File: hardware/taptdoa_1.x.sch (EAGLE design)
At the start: 67 parts, among them J1 105017-0001, U1 AP2112K-3.3TRG1, U2 STM32F103RBT6, Y1 8MHz

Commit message: v1.2 of board
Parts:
- removed TP21, TP22, TP4, TP5, TP6, TP7: TEST-POINT3X4, SparkFun-Connectors:TEST-POINT3X4
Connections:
- removed net PC0: R1.1, U2.PC0
- removed net PC1: R2.1, U2.PC1
- removed net PC2: R5.1, U2.PC2
- removed net PC3: R3.1, U2.PC3
- removed net PC4: R4.1, U2.PC4
- removed net PC5: R6.1, U2.PC5
- net OPAMP3_OUT: now also TP2.1; no longer TP21.1
- net PB2: now also TP3.1; no longer TP22.1
- net PB3: now also R1.1; no longer TP7.1
- net PB4: now also R2.1; no longer TP6.1
- net PB5: now also R5.1; no longer TP5.1
- net PB6: now also R3.1; no longer TP4.1
- net PB7: now also R4.1; no longer TP3.1
- net PB8: now also R6.1; no longer TP2.1
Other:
- moved on the sheet: C5, C9, J2, R1, R2, R3, R4, R5, R6, TP2, TP3

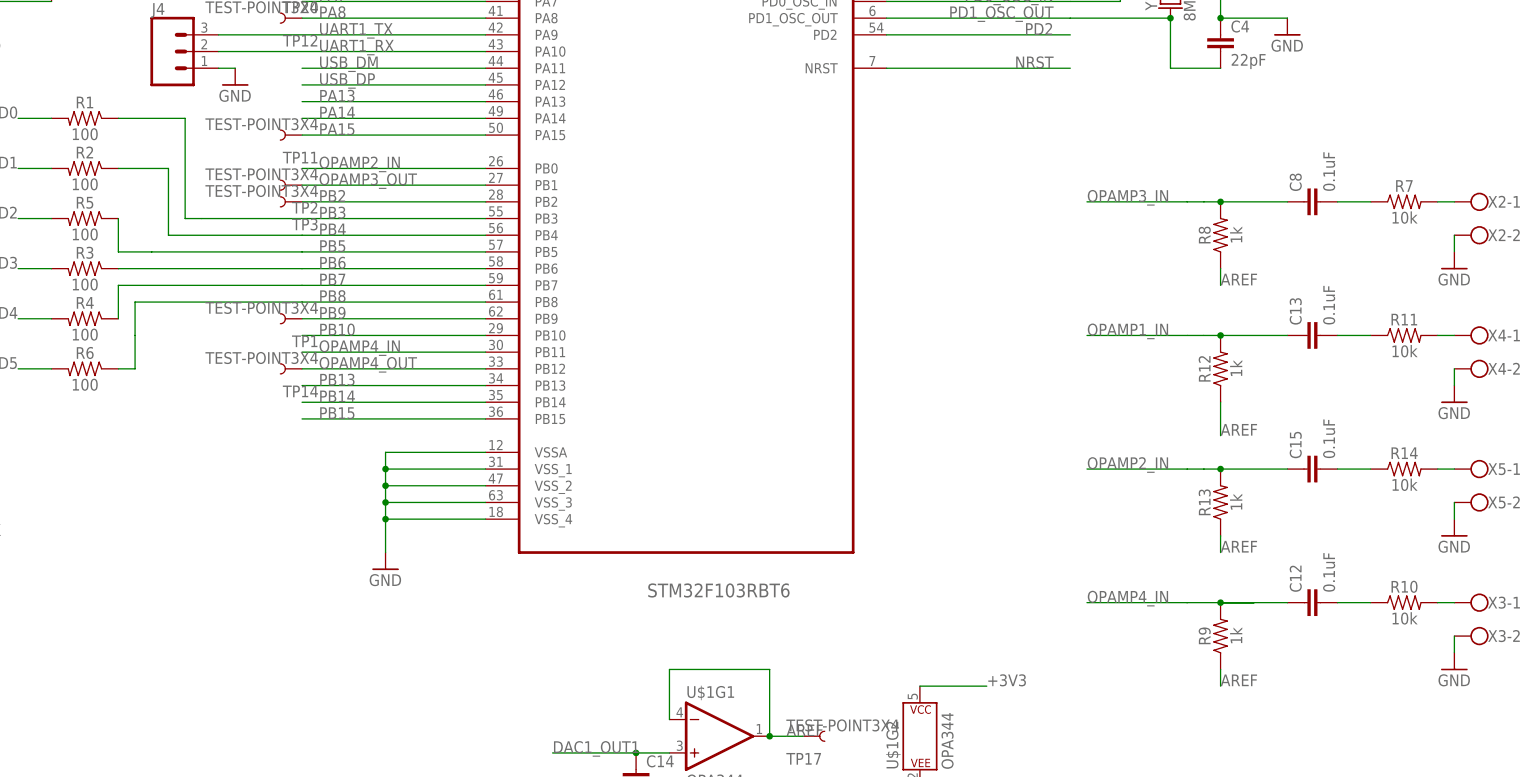
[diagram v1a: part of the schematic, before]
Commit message: working on LEDs, simple threshold detection for now, limited filtering
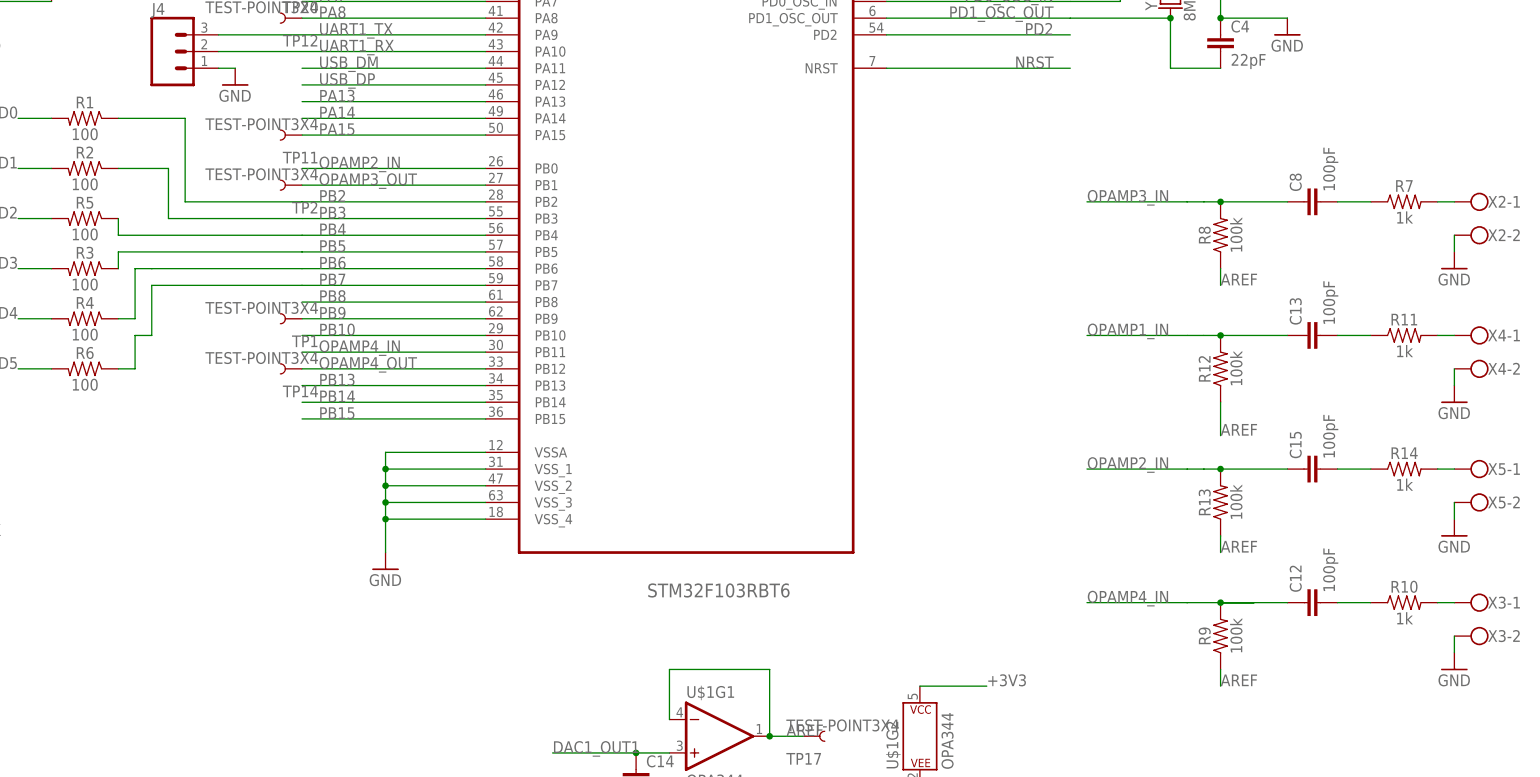
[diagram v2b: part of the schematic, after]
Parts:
- removed TP3: TEST-POINT3X4, SparkFun-Connectors:TEST-POINT3X4
- C12, C13, C15, C8: value 0.1uF -> 100pF
- R10, R11, R14, R7: value 10k -> 1k
- R12, R13, R8, R9: value 1k -> 100k
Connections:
- net PB2: now also R1.1; no longer TP3.1
- net PB3: now also R2.1; no longer R1.1
- net PB4: now also R5.1; no longer R2.1
- net PB5: now also R3.1; no longer R5.1
- net PB6: now also R4.1; no longer R3.1
- net PB7: now also R6.1; no longer R4.1
- net PB8: no longer R6.1

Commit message: re layout board
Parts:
- removed C14: 0.1uF, SparkFun-Capacitors:0.1UF-0603-25V-5%
- removed TP13, TP14, TP15, TP16, TP18, TP19, TP20: TEST-POINT3X4, SparkFun-Connectors:TEST-POINT3X4
- removed X1, X2, X3, X4, X5: (no value), con-wago-500:W237-102
- added C16: 0.1uF, SparkFun-Capacitors:0.1UF-0603-25V-5%
- added C17: 1.0uF, SparkFun-Capacitors:1.0UF-0603-16V-10%
- added C18, C19, C20, C21, C22, C23, C24, C25: 1nF, SparkFun-Capacitors:1.0UF-0603-16V-10%
- added C26, C27: 100uF, SparkFun-Capacitors:100UF-POLAR-25V-20%(ELEC)
- added FB2, FB3, FB4, FB5, FB6: 30Ω/1.8A, SparkFun-Coils:FERRITE_BEAD-0603
- added J6, J7: (no value), SparkFun-Connectors:CONN_04LOCK_LONGPADS
- added L1: 3.3µH/±20%/450mA, SparkFun-Coils:INDUCTOR-0805-3.3UH
- added R16, R17: 33, SparkFun-Resistors:100OHM-0603-1/4W-5%
- added R18, R19: 75, SparkFun-Resistors:100OHM-0603-1/4W-5%
- added TP3, TP4, TP5, TP6, TP7: TEST-POINT3X4, SparkFun-Connectors:TEST-POINT3X4
- added U$2: XT30XT30_THRUHOLE, XT30Male:XT30XT30_THRUHOLE
- added U4: SN74HCT245PWR, scanlime:74245PW
- C12, C13, C15, C8: value 100pF -> 1nF
- C3: value 1.0uF -> 4.7uF
- J3: device SparkFun-Connectors:CONN_09LOCK-LONGPADS -> SparkFun-Connectors:CONN_18
- J5: device SparkFun-Connectors:CONN_09LOCK-LONGPADS -> SparkFun-Connectors:CONN_06LOCK
- R1, R2, R3, R4, R5, R6: value 100 -> 75
- R10, R11, R14, R7: value 1k -> 10k
- R12, R13, R8, R9: value 100k -> 10k
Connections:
- removed net +5V: J3.3, J3.6, J3.9, J5.3, J5.6, J5.9, X1-1.KL
- removed net DAC1_OUT2: TP19.1, U2.PA5
- removed net N$1: R7.2, X2-1.KL
- removed net N$3: R11.2, X4-1.KL
- removed net N$5: R14.2, X5-1.KL
- removed net N$7: C12.2, R10.1
- removed net OPAMP1_IN: C13.1, R12.2, U2.PA3
- removed net OPAMP1_OUT: TP18.1, U2.PA2
- removed net OPAMP2_IN: C15.1, R13.2, U2.PB0
- removed net OPAMP2_OUT: TP20.1, U2.PA6
- removed net OPAMP3_IN: C8.1, R8.2, U2.PA1
- removed net OPAMP3_OUT: TP2.1, U2.PB1
- removed net OPAMP4_IN: C12.1, R9.2, U2.PB11
- removed net OPAMP4_OUT: TP14.1, U2.PB12
- removed net PA0-WKUP: U2.PA0-WKUP
- removed net PA15: TP11.1, U2.PA15
- removed net PA7: U2.PA7
- removed net PA8: TP12.1, U2.PA8
- removed net PB10: U2.PB10
- removed net PB13: U2.PB13
- removed net PB14: U2.PB14
- removed net PB15: U2.PB15
- removed net PB2: R1.1, U2.PB2
- removed net PB3: R2.1, U2.PB3
- removed net PB4: R5.1, U2.PB4
- removed net PB5: R3.1, U2.PB5
- removed net PB6: R4.1, U2.PB6
- removed net PB7: R6.1, U2.PB7
- removed net PB8: U2.PB8
- removed net PB9: TP1.1, U2.PB9
- removed net PC10: TP10.1, U2.PC10
- removed net PC11: TP9.1, U2.PC11
- removed net PC12: TP8.1, U2.PC12
- removed net PC13-TAMPER-RTC: U2.PC13-TAMPER-RTC
- removed net PC14-OSC32_IN: U2.PC14-OSC32_IN
- removed net PC15-OSC32_OUT: U2.PC15-OSC32_OUT
- removed net PC6: TP16.1, U2.PC6
- removed net PC7: TP13.1, U2.PC7
- removed net PC8: TP15.1, U2.PC8
- removed net PC9: U2.PC9
- removed net PD2: U2.PD2
- removed net VBAT: U2.VBAT
- new net 5V: C26.+, C27.+, J3.1, J3.10, J3.13, J3.16, J3.4, J3.7, J5.1, J5.4, U$2.5V, U4.DIR, U4.VCC
- new net HP1: C8.1, R7.2, R8.2, TP9.1
- new net HP2: C13.1, R11.2, R12.2, TP10.1
- new net HP3: C15.1, R13.2, R14.2, TP11.1
- new net HP4: C12.1, R10.2, R9.2, TP12.1
- new net N$10: R17.1, U2.PA12
- new net N$11: FB2.1, J1.GND
- new net N$12: C17.1, L1.1, U1.OUT
- new net N$13: R1.1, U4.B1
- new net N$14: R2.1, U4.B2
- new net N$15: R5.1, U4.B3
- new net N$16: R3.1, U4.B4
- new net N$17: R4.1, U4.B5
- new net N$18: R6.1, U4.B6
- new net N$19: C8.2, FB3.1
- new net N$20: C15.2, FB5.1
- new net N$21: C13.2, FB4.1
- new net N$22: U2.PC12, U4.A4
- new net N$23: C12.2, FB6.1
- new net N$24: U2.PC13-TAMPER-RTC, U4.A3
- new net N$25: U2.PC14-OSC32_IN, U4.A2
- new net N$26: U2.PC15-OSC32_OUT, U4.A1
- new net N$27: R18.1, U4.B7
- new net N$28: R19.1, U4.B8
- new net N$29: J5.2, R18.2
- new net N$30: J5.5, R19.2
- new net N$31: FB3.2, J6.1
- new net N$32: FB5.2, J7.1
- new net N$33: FB6.2, J7.3
- new net N$34: FB4.2, J6.3
- new net N$9: R16.1, U2.PA11
- new net OA1NEG: C22.1, U2.PA3
- new net OA1OUT: C22.2, TP4.1, U2.PA2
- new net OA2NEG: C23.1, U2.PC5
- new net OA2OUT: C23.2, TP3.1, U2.PA6
- new net OA3NEG: C24.1, U2.PB2
- new net OA3OUT: C24.2, TP1.1, U2.PB1
- new net OA4NEG: C25.2, U2.PB10
- new net OA4OUT: C25.1, TP2.1, U2.PB12
- new net SENSE1: C18.2, R7.1, TP8.1, U2.PA0-WKUP, U2.PA1
- new net SENSE2: C19.2, R11.1, TP7.1, U2.PA7, U2.PC4
- new net SENSE3: C20.2, R14.1, TP6.1, U2.PB0, U2.PB13
- new net SENSE4: C21.2, R10.1, TP5.1, U2.PB11, U2.PB14
- net +3V3: now also L1.2; no longer U1.OUT
- net AREF: now also C18.1, C19.1, C20.1, C21.1
- net DAC1_OUT1: no longer C14.1
- net GND: now also C16.2, C17.2, C26.-, C27.-, FB2.2, J3.12, J3.15, J3.18, J3.3, J3.6, J3.9, J5.3, J5.6, J6.2, J6.4, J7.2, J7.4, U$2.GND, U4.GND, U4.OE; no longer C14.2, J1.GND, J3.1, J3.4, J3.7, J5.1, J5.4, J5.7, X1-2.KL, X2-2.KL, X3-2.KL, X4-2.KL, X5-2.KL
- net LED0: now also J3.2; no longer J3.8
- net LED2: now also J3.8; no longer J3.2
- net LED3: now also J3.11; no longer J5.8
- net LED4: now also J3.14; no longer J5.5
- net LED5: now also J3.17; no longer J5.2
- net N$2: now also U2.PC8, U4.A8; no longer C13.2, R11.1
- net N$4: now also U2.PC9, U4.A7; no longer C15.2, R14.1
- net N$6: now also U2.PC10, U4.A6; no longer R10.2, X3-1.KL
- net N$8: now also U2.PC11, U4.A5; no longer C8.2, R7.1
- net PA13: now also U2.PA15; no longer U2.PA13
- net USB_DM: now also R16.2; no longer U2.PA11
- net USB_DP: now also R17.2; no longer U2.PA12
- net VUSB2: now also C16.1
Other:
- note added: "Serial"
- moved on the sheet: C1, C12, C13, C15, C3, C4, C5, C7, C8, C9, J2, J4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

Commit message: cleanup renumber
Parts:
- removed C27: 100uF, SparkFun-Capacitors:100UF-POLAR-25V-20%(ELEC)
- removed TP17: TEST-POINT3X4, SparkFun-Connectors:TEST-POINT3X4
- removed U4: SN74HCT245PWR, scanlime:74245PW
- added C14: 1nF, SparkFun-Capacitors:1.0UF-0603-16V-10%
- added TP13: TEST-POINT3X4, SparkFun-Connectors:TEST-POINT3X4
- added U3: STM32F103RBT6, ST Microelctronics_By_element14_Batch_1:STM32F103RBT6
- C1: value 22pF -> 100uF; device SparkFun-Capacitors:22PF-0603-50V-5% -> SparkFun-Capacitors:100UF-POLAR-25V-20%(ELEC)
- C10: value 0.1uF -> 10nF; device SparkFun-Capacitors:0.1UF-0603-25V-5% -> SparkFun-Capacitors:10NF-0603-50V-10%
- C11: value 0.1uF -> 1.0uF; device SparkFun-Capacitors:0.1UF-0603-25V-5% -> SparkFun-Capacitors:1.0UF-0603-16V-10%
- C13, C19, C22: value 1nF -> 0.1uF; device SparkFun-Capacitors:1.0UF-0603-16V-10% -> SparkFun-Capacitors:0.1UF-0603-25V-5%
- C16: value 0.1uF -> 1nF; device SparkFun-Capacitors:0.1UF-0603-25V-5% -> SparkFun-Capacitors:1.0UF-0603-16V-10%
- C17: value 1.0uF -> 1nF
- C2: value 0.1uF -> 100uF; device SparkFun-Capacitors:0.1UF-0603-25V-5% -> SparkFun-Capacitors:100UF-POLAR-25V-20%(ELEC)
- C26: value 100uF -> 1nF; device SparkFun-Capacitors:100UF-POLAR-25V-20%(ELEC) -> SparkFun-Capacitors:1.0UF-0603-16V-10%
- C3: value 4.7uF -> 0.1uF; device SparkFun-Capacitors:1.0UF-0603-16V-10% -> SparkFun-Capacitors:0.1UF-0603-25V-5%
- C4: value 22pF -> 4.7uF; device SparkFun-Capacitors:22PF-0603-50V-5% -> SparkFun-Capacitors:4.7UF0603
- C5: value 10nF -> 1.0uF; device SparkFun-Capacitors:10NF-0603-50V-10% -> SparkFun-Capacitors:1.0UF-0603-16V-10%
- C6: value 0.1uF -> 4.7uF; device SparkFun-Capacitors:0.1UF-0603-25V-5% -> SparkFun-Capacitors:1.0UF-0603-16V-10%
- C7: value 4.7uF -> 0.1uF; device SparkFun-Capacitors:4.7UF0603 -> SparkFun-Capacitors:0.1UF-0603-25V-5%
- C8: value 1nF -> 22pF; device SparkFun-Capacitors:1.0UF-0603-16V-10% -> SparkFun-Capacitors:22PF-0603-50V-5%
- C9: value 1.0uF -> 22pF; device SparkFun-Capacitors:1.0UF-0603-16V-10% -> SparkFun-Capacitors:22PF-0603-50V-5%
- J1: value 105017-0001 -> (none); device molex usb 105017-0001:105017-0001 -> SparkFun-Connectors:CONN_18
- J2: device SparkFun-Connectors:CONN_05LOCK -> SparkFun-Connectors:CONN_06LOCK
- J3: device SparkFun-Connectors:CONN_18 -> SparkFun-Connectors:CONN_05LOCK
- J5: value (none) -> 105017-0001; device SparkFun-Connectors:CONN_06LOCK -> molex usb 105017-0001:105017-0001
- R10, R9: value 10k -> 33; device SparkFun-Resistors:RESISTOR0603 -> SparkFun-Resistors:100OHM-0603-1/4W-5%
- R11: value 10k -> 4.7k
- R15: value 4.7k -> 10k
- R16, R17: value 33 -> 10k; device SparkFun-Resistors:100OHM-0603-1/4W-5% -> SparkFun-Resistors:RESISTOR0603
- R18, R19: value 75 -> 10k; device SparkFun-Resistors:100OHM-0603-1/4W-5% -> SparkFun-Resistors:RESISTOR0603
- R7, R8: value 10k -> 75; device SparkFun-Resistors:RESISTOR0603 -> SparkFun-Resistors:100OHM-0603-1/4W-5%
- U$1: value OPA344 -> XT30XT30_THRUHOLE; device SparkFun-IC-Amplifiers:OPA344 -> XT30Male:XT30XT30_THRUHOLE
- U$2: value XT30XT30_THRUHOLE -> OPA344; device XT30Male:XT30XT30_THRUHOLE -> SparkFun-IC-Amplifiers:OPA344
- U1: value AP2112K-3.3TRG1 -> SN74HCT245PWR; device SparkFun-PowerIC:V_REG_AP2112K-3.3V -> scanlime:74245PW
- U2: value STM32F103RBT6 -> AP2112K-3.3TRG1; device ST Microelctronics_By_element14_Batch_1:STM32F103RBT6 -> SparkFun-PowerIC:V_REG_AP2112K-3.3V
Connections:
- net +3V3: now also C13.1, C19.1, C22.1, C3.1, C4.1, J3.5, U$2G2.P$V+, U3.VDDA, U3.VDD_1, U3.VDD_2, U3.VDD_3, U3.VDD_4; no longer C2.1, C5.1, C6.1, C7.1, C9.1, J2.5, U$1G2.P$V+, U2.VDDA, U2.VDD_1, U2.VDD_2, U2.VDD_3, U2.VDD_4
- net 5V: now also C1.+, C2.+, J1.1, J1.10, J1.13, J1.16, J1.4, J1.7, J2.1, J2.4, U$1.5V, U1.DIR, U1.VCC; no longer C26.+, C27.+, J3.1, J3.10, J3.13, J3.16, J3.4, J3.7, J5.1, J5.4, U$2.5V, U4.DIR, U4.VCC
- net AREF: now also C16.1, C17.1, C23.1, C24.1, R17.1, R18.1, R19.1, TP8.1, U$2G1.-IN, U$2G1.OUT; no longer C18.1, C19.1, C20.1, C21.1, R13.1, R8.1, R9.1, TP17.1, U$1G1.-IN, U$1G1.OUT
- net DAC1_OUT1: now also U$2G1.+IN, U3.PA4; no longer U$1G1.+IN, U2.PA4
- net GND: now also C1.-, C13.2, C19.2, C2.-, C22.2, C4.2, C8.2, C9.1, FB1.2, J1.12, J1.15, J1.18, J1.3, J1.6, J1.9, J2.6, U$1.GND, U$2G2.P$V-, U1.OE, U2.GND, U3.BOOT0, U3.VSSA, U3.VSS_1, U3.VSS_2, U3.VSS_3, U3.VSS_4; no longer C1.2, C16.2, C17.2, C2.2, C26.-, C27.-, C4.1, C9.2, FB2.2, J3.12, J3.15, J3.18, J3.6, J3.9, J5.3, J5.6, U$1G2.P$V-, U$2.GND, U2.BOOT0, U2.VSSA, U2.VSS_1, U2.VSS_2, U2.VSS_3, U2.VSS_4, U4.GND, U4.OE
- net HP1: now also C14.1, R12.2, R13.2, TP2.1; no longer C8.1, R7.2, R8.2, TP9.1
- net HP2: now also C15.1, R14.2, R19.2, TP3.1; no longer C13.1, R11.2, R12.2, TP10.1
- net HP3: now also C26.1, R16.2, R18.2, TP12.1; no longer C15.1, R13.2, R14.2, TP11.1
- net HP4: now also C25.1, R15.2, R17.2, TP13.1; no longer C12.1, R10.2, R9.2, TP12.1
- net ID: now also J5.ID; no longer J1.ID
- net LED0: now also J1.2; no longer J3.2
- net LED1: now also J1.5; no longer J3.5
- net LED2: now also J1.8, R3.2; no longer J3.8, R5.2
- net LED3: now also J1.11, R4.2; no longer J3.11, R3.2
- net LED4: now also J1.14, R5.2; no longer J3.14, R4.2
- net LED5: now also J1.17; no longer J3.17
- net N$10: now also R9.1, U3.PA12; no longer R17.1, U2.PA12
- net N$11: now also FB1.1, J5.GND; no longer FB2.1, J1.GND
- net N$12: now also C5.1, U2.OUT; no longer C17.1, U1.OUT
- net N$13: now also U1.B1; no longer U4.B1
- net N$14: now also U1.B2; no longer U4.B2
- net N$15: now also R3.1, U1.B3; no longer R5.1, U4.B3
- net N$16: now also R4.1, U1.B4; no longer R3.1, U4.B4
- net N$17: now also R5.1, U1.B5; no longer R4.1, U4.B5
- net N$18: now also U1.B6; no longer U4.B6
- net N$19: now also C14.2; no longer C8.2
- net N$2: now also U1.A8, U3.PC8; no longer U2.PC8, U4.A8
- net N$20: now also C26.2, FB6.1; no longer C15.2, FB5.1
- net N$21: now also C15.2; no longer C13.2
- net N$22: now also U1.A4, U3.PC12; no longer U2.PC12, U4.A4
- net N$23: now also C25.2, FB5.1; no longer C12.2, FB6.1
- net N$24: now also U1.A3, U3.PC13-TAMPER-RTC; no longer U2.PC13-TAMPER-RTC, U4.A3
- net N$25: now also U1.A2, U3.PC14-OSC32_IN; no longer U2.PC14-OSC32_IN, U4.A2
- net N$26: now also U1.A1, U3.PC15-OSC32_OUT; no longer U2.PC15-OSC32_OUT, U4.A1
- net N$27: now also R7.1, U1.B7; no longer R18.1, U4.B7
- net N$28: now also R8.1, U1.B8; no longer R19.1, U4.B8
- net N$29: now also J2.2, R7.2; no longer J5.2, R18.2
- net N$30: now also J2.5, R8.2; no longer J5.5, R19.2
- net N$32: now also FB6.2; no longer FB5.2
- net N$33: now also FB5.2; no longer FB6.2
- net N$4: now also U1.A7, U3.PC9; no longer U2.PC9, U4.A7
- net N$6: now also U1.A6, U3.PC10; no longer U2.PC10, U4.A6
- net N$8: now also U1.A5, U3.PC11; no longer U2.PC11, U4.A5
- net N$9: now also R10.1, U3.PA11; no longer R16.1, U2.PA11
- net NRST: now also J3.1, U3.NRST; no longer J2.1, U2.NRST
- net OA1NEG: now also C18.1, U3.PA3; no longer C22.1, U2.PA3
- net OA1OUT: now also C18.2, TP6.1, U3.PA2; no longer C22.2, TP4.1, U2.PA2
- net OA2NEG: now also C20.1, U3.PC5; no longer C23.1, U2.PC5
- net OA2OUT: now also C20.2, TP7.1, U3.PA6; no longer C23.2, TP3.1, U2.PA6
- net OA3NEG: now also C21.1, U3.PB2; no longer C24.1, U2.PB2
- net OA3OUT: now also C21.2, TP9.1, U3.PB1; no longer C24.2, TP1.1, U2.PB1
- net OA4NEG: now also C12.2, U3.PB10; no longer C25.2, U2.PB10
- net OA4OUT: now also C12.1, TP1.1, U3.PB12; no longer C25.1, TP2.1, U2.PB12
- net PA13: now also J3.2, U3.PA15; no longer J2.2, U2.PA15
- net PA14: now also J3.4, U3.PA14; no longer J2.4, U2.PA14
- net PD0_OSC_IN: now also C8.1, U3.PD0_OSC_IN; no longer C1.1, U2.PD0_OSC_IN
- net PD1_OSC_OUT: now also C9.2, U3.PD1_OSC_OUT; no longer C4.2, U2.PD1_OSC_OUT
- net SENSE1: now also C16.2, R13.1, TP4.1, U3.PA0-WKUP, U3.PA1; no longer C18.2, R7.1, TP8.1, U2.PA0-WKUP, U2.PA1
- net SENSE2: now also C17.2, R14.1, TP5.1, U3.PA7, U3.PC4; no longer C19.2, R11.1, TP7.1, U2.PA7, U2.PC4
- net SENSE3: now also C24.2, R16.1, TP10.1, U3.PB0, U3.PB13; no longer C20.2, R14.1, TP6.1, U2.PB0, U2.PB13
- net SENSE4: now also C23.2, R15.1, TP11.1, U3.PB11, U3.PB14; no longer C21.2, R10.1, TP5.1, U2.PB11, U2.PB14
- net UART1_RX: now also U3.PA10; no longer U2.PA10
- net UART1_TX: now also U3.PA9; no longer U2.PA9
- net USB_DM: now also J5.D-, R10.2; no longer J1.D-, R16.2
- net USB_DP: now also J5.D+, R11.1, R9.2; no longer J1.D+, R15.1, R17.2
- net VUSB: now also FB2.1, J5.VDD, R11.2; no longer FB1.1, J1.VDD, R15.2
- net VUSB2: now also C6.1, C7.1, FB2.2, U2.EN, U2.IN; no longer C16.1, C3.1, FB1.2, U1.EN, U1.IN
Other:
- moved on the sheet: C10, C11, C12, C13, C15, C16, C17, C18, C19, C20, C21, C22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
